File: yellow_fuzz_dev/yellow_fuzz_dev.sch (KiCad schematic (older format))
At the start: 150 parts

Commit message: woo boy I dunno buncha progress probably
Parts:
- removed C?: 27n, Capacitor_SMD:C_0603_1608Metric_Pad1.05x0.95mm_HandSolder, symbol Device:C
- removed C? (x2): 10n, Capacitor_SMD:C_0603_1608Metric_Pad1.05x0.95mm_HandSolder, symbol Device:C
- removed C?: 10p, Capacitor_SMD:C_0603_1608Metric_Pad1.05x0.95mm_HandSolder, symbol Device:C
- removed C? (x2): 1u, symbol Device:CP1
- removed C?: 100p, Capacitor_SMD:C_0603_1608Metric_Pad1.05x0.95mm_HandSolder, symbol Device:C
- removed C?: 220n, symbol Device:CP1
- removed C?: 47n, Capacitor_SMD:C_0603_1608Metric_Pad1.05x0.95mm_HandSolder, symbol Device:C
- removed C? (x3): 0.1u, Capacitor_SMD:C_0603_1608Metric_Pad1.05x0.95mm_HandSolder, symbol Device:C
- removed C?: 8.2n, Capacitor_SMD:C_0603_1608Metric_Pad1.05x0.95mm_HandSolder, symbol Device:C
- removed C?: 22n, Capacitor_SMD:C_0603_1608Metric_Pad1.05x0.95mm_HandSolder, symbol Device:C
- removed C?: 10u, symbol Device:CP1
- removed J?: PJ-202A, CUI_PJ-202A, symbol PJ-202A:PJ-202A
- removed R? (x3): 47k, Resistor_SMD:R_0603_1608Metric_Pad1.05x0.95mm_HandSolder, symbol Device:R
- removed R? (x5): 2.2k, Resistor_SMD:R_0603_1608Metric_Pad1.05x0.95mm_HandSolder, symbol Device:R
- removed R?: 22k, Resistor_SMD:R_0603_1608Metric_Pad1.05x0.95mm_HandSolder, symbol Device:R
- removed R? (x2): 330, Resistor_SMD:R_0603_1608Metric_Pad1.05x0.95mm_HandSolder, symbol Device:R
- removed R?: 100k, Resistor_SMD:R_0603_1608Metric_Pad1.05x0.95mm_HandSolder, symbol Device:R
- removed R?: 1M, Resistor_SMD:R_0603_1608Metric_Pad1.05x0.95mm_HandSolder, symbol Device:R
- removed RV?: R_POT_US, yellow_fuzz_dev:Potentiometer_Bourns_PCW1J_R24_B_Single_Vertical, symbol Device:R_POT_US
- removed RV? (x2): R_POT_Dual_Separate, yellow_fuzz_dev:Potentiometer_Bourns_PTV112_3417A_Dual_Vertical, symbol Device:R_POT_Dual_Separate
- removed RV? (x3): R_POT_US, yellow_fuzz_dev:Potentiometer_Bourns_PTV111_4420A_Single_Vertical, symbol Device:R_POT_US
- removed U? (x4): TL072CP, digikey-footprints:DIP-8_W7.62mm, symbol dk_opamps:TL072CP
- added C?: 10n, Capacitor_SMD:C_0603_1608Metric_Pad1.05x0.95mm_HandSolder, symbol Device:C
- added C?: 27n, Capacitor_SMD:C_0603_1608Metric_Pad1.05x0.95mm_HandSolder, symbol Device:C
- added C?: 0.1u, Capacitor_SMD:C_0603_1608Metric_Pad1.05x0.95mm_HandSolder, symbol Device:C
- added C?: 47n, Capacitor_SMD:C_0603_1608Metric_Pad1.05x0.95mm_HandSolder, symbol Device:C
- added J?: PJ-202A, digikey-footprints:Barrel_Jack_5.5mmODx2.1mmID_PJ-202A, symbol dk_Barrel-Power-Connectors:PJ-202A
- added Q?: BC817-25-TP, digikey-footprints:SOT-23-3, symbol yellow_fuzz_dev-rescue:BC817-25-TP-dk_NPN_Single
- added R?: 10k, Resistor_SMD:R_0603_1608Metric_Pad1.05x0.95mm_HandSolder, symbol Device:R
- added R? (x2): 2.2k, Resistor_SMD:R_0603_1608Metric_Pad1.05x0.95mm_HandSolder, symbol Device:R
- added R? (x2): 47k, Resistor_SMD:R_0603_1608Metric_Pad1.05x0.95mm_HandSolder, symbol Device:R
- added R?: 1k, Resistor_SMD:R_0603_1608Metric_Pad1.05x0.95mm_HandSolder, symbol Device:R
- added SW?: SW_SP3T_A24JP, yellow_fuzz_dev:A24JP, symbol yellow_fuzz_dev:SW_SP3T_A24JP
- added SW? (x2): SW_SPST_A11JP, yellow_fuzz_dev:A11JP, symbol yellow_fuzz_dev:SW_SPST_A11JP
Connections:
- net labels removed: LEVEL_OUT, TONE_IN, TONE_OUT
- wire segments 476 -> 389
- no-connect marks 0 -> 1
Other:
- note added: "333 Hz, Q = 4.6"
- note added: "4.9 kHz, Q = 2.2"
- note added: "First-order BPF (6 dB of cut at fc). \nfc = 200 Hz."
- note added: "HPF fc = 5 Hz"
- note added: "Returned pre-distortion boost:\n36dB centered at 224Hz, Q = 3.2."
- note added: "Stock pre-distortion boost:\n36dB centered at 1kHz, Q = 2.8."
- note added: "Three-position toggle implements \nSP3T when pins 3 and 5 are connected.\n\nUnused position removes filter from preboost."
- note added: "Tone"
- note added: "fc = 4 Hz"
- note removed: "High"
- note removed: "Level\n"
- note removed: "Low"
- note removed: "Mid Freq\n"
- note removed: "Mid\n"
- note removed: "Retuned pre-distortion boost filter."
- moved on the sheet: C?, D?, Q?, R?, RV?, S?, U?A, U?B

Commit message: moved footprints into PCB
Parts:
- removed C? (x3): 10u, symbol Device:CP1
- removed C? (x3): 1u, symbol Device:CP1
- removed C?: 100u, symbol Device:CP1
- removed R?: 220k, Resistor_SMD:R_0603_1608Metric_Pad1.05x0.95mm_HandSolder, symbol Device:R
- added C12: 100u, Capacitor_THT:CP_Radial_D5.0mm_P2.00mm, symbol Device:CP1
- added C17, C34, C37: 10u, Capacitor_THT:CP_Radial_D5.0mm_P2.00mm, symbol Device:CP1
- added C19, C26, C36: 1u, Capacitor_THT:CP_Radial_D4.0mm_P1.50mm, symbol Device:CP1
- added D5, D8: 1N34A, digikey:DO-35, symbol dk_Diodes-Rectifiers-Single:1N914BTR
- added D6, D9: WP7113QBC_D, digikey:LED_5mm_Radial, symbol yellow_fuzz_dev-rescue:WP7113QBC_D-dk_LEDs
- added POT1: 3386P-1-204TLF, yellow_fuzz_dev:3386P, symbol yellow_fuzz_dev:3386P-1-204TLF
- added POT2, POT3: 3362P-1-102TLF, yellow_fuzz_dev:3362P-1-102TLF, symbol yellow_fuzz_dev:3362P-1-102TLF
- added R16: 1k, Resistor_SMD:R_0603_1608Metric_Pad1.05x0.95mm_HandSolder, symbol Device:R
- added SW2, SW3: SW_SP3T_A24JP, yellow_fuzz_dev:A24JP, symbol yellow_fuzz_dev:SW_SP3T_A24JP
- BAT1: renamed from BAT?; footprint digikey-footprints:Battery_Holder_9V_BC9VPC-ND -> digikey:Battery_Holder_9V_BC9VPC-ND
- C1: renamed from C?; footprint (none) -> Capacitor_THT:CP_Radial_D4.0mm_P1.50mm
- C11, C15, C22, C8: renamed from C?; footprint (none) -> Capacitor_THT:CP_Radial_D5.0mm_P2.00mm
- CON1: renamed from CON?; footprint digikey-footprints:Headphone_Jack_6.35mm_SN49B12B -> digikey:Headphone_Jack_6.35mm_SN49B12B
- D3: renamed from D?; footprint digikey-footprints:LED_5mm_Radial -> digikey:LED_5mm_Radial
- D4, D7: renamed from D?; footprint digikey-footprints:Diode_DO-35_P10mm -> digikey:Diode_DO-35_P10mm
- J1: renamed from J?; footprint digikey-footprints:Barrel_Jack_5.5mmODx2.1mmID_PJ-202A -> digikey:Barrel_Jack_5.5mmODx2.1mmID_PJ-202A
- Q10, Q12, Q13, Q5, Q6, Q7, Q8, Q9: renamed from Q?; footprint digikey-footprints:SOT-23-3 -> digikey:SOT-23-3
- S1: renamed from S?; footprint digikey-footprints:Switch_Tactile_THT_6x6mm -> digikey:Switch_Tactile_THT_6x6mm
- U1, U2: renamed from U?; footprint digikey-footprints:DIP-8_W7.62mm -> digikey:DIP-8_W7.62mm
- gave numbers to parts that had none: 94
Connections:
- net +4V: now also C12.1
- net GND: now also C12.2, D5.K, D6.2, D8.A, D9.1
- net tone_block/TONE_OUT: now also C36.2
- net at C16.1, RV1.2, RV1.3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: now also C17.1
- net at C9.1, R17.2, U1.1: now also R16.1
- net at C9.2, SW1.2, U1.2: now also POT1.1 (CCW), POT1.2 (S)
- net at R23.2: now also C17.2
- net at R23.1, R26.2: now also POT2.1 (CCW), POT3.1 (CCW); no longer D4.2, D7.1
- net at R26.1, R27.1: now also C19.2
- net at R32.2, U2.3: now also C19.1
- net at Q9.2 (E), R35.1: now also C26.1
- net at Q11.1 (S), R40.2: now also C26.2
- net at Q13.1 (B), R48.2: now also C34.1
- net at Q11.2 (D), Q14.2 (D), R55.2: now also C34.2
- net at Q13.2 (E), R51.1: now also C37.1
- net at R53.1, R54.2: now also C37.2
- net at Q14.1 (S), R52.2: now also C36.1
- new net: D4.2, SW2.1
- new net: D7.1, SW3.1
- new net: POT2.2 (S), POT2.3 (CW), SW2.2
- new net: POT3.2 (S), POT3.3 (CW), SW3.2
- new net: POT1.3 (CW), R16.2
- new net: SW2.3, SW2.5
- new net: D5.A, SW2.4
- new net: D6.1, SW2.6
- new net: SW3.3, SW3.5
- new net: D8.K, SW3.4
- new net: D9.2, SW3.6
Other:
- note added: "200k Trim Pot lets us turn down the preboost, \nallowing us to take out op-amp clipping as much as we’d like."
- note added: "Let’s see if this takes the fizz out maybe."
- note added: "Three-position toggle implements \nSP3T when pins 3 and 5 are connected.\n\nNow you can A/B/C test diodes."
- moved on the sheet: C28, C29, C30, C31, C33, C35, D4, D7, Q10, Q12, R37, R39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

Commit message: added 3d to connector and DIP footprints, moved to project lib, updated PCB
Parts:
- removed BAT1: BC9VPC, digikey:Battery_Holder_9V_BC9VPC-ND, symbol dk_Battery-Holders-Clips-Contacts:BC9VPC
- removed CON1: SN49B12B, digikey:Headphone_Jack_6.35mm_SN49B12B, symbol yellow_fuzz_dev-rescue:SN49B12B-dk_Barrel-Audio-Connectors
- removed J1: PJ-202A, digikey:Barrel_Jack_5.5mmODx2.1mmID_PJ-202A, symbol dk_Barrel-Power-Connectors:PJ-202A
- removed POT2, POT3: 3362P-1-102TLF, yellow_fuzz_dev:3362P-1-102TLF, symbol yellow_fuzz_dev:3362P-1-102TLF
- removed S1: 1825910-6, digikey:Switch_Tactile_THT_6x6mm, symbol dk_Tactile-Switches:1825910-6
- removed U1, U2: TL072CP, digikey:DIP-8_W7.62mm, symbol dk_opamps:TL072CP
- added BAT1: BC9VPC, yellow_fuzz_dev:Battery_Holder_9V_BC9VPC-ND, symbol yellow_fuzz_dev:BC9VPC
- added J1: PJ-202A, yellow_fuzz_dev:Barrel_Jack_5.5mmODx2.1mmID_PJ-202A, symbol yellow_fuzz_dev:PJ-202A
- added J3: SN49B12B, yellow_fuzz_dev:Headphone_Jack_6.35mm_SN49B12B, symbol yellow_fuzz_dev:SN49B12B
- added P3, P4: 3362P-1-102TLF, yellow_fuzz_dev:3362PT, symbol yellow_fuzz_dev:3362P-1-102TLF
- added S1: 1825910-6, yellow_fuzz_dev:Switch_Tactile_THT_6x6mm, symbol yellow_fuzz_dev:1825910-6
- added U1, U2: TL072CP, yellow_fuzz_dev:DIP-8_W7.62mm, symbol yellow_fuzz_dev:TL072CP
- J2: Manufacturer Switchcraft Inc. -> (none); Manufacturer PN RA49B11 -> (none); Supplier Digi-Key -> (none); Supplier PN SC2546-ND -> (none)
- renumbered POT1 to P1, RV1 to P2
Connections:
- net +4V: now also U2.5
- net +9V: now also U1.8 (VCC+), U1.8 (VCC+), U2.8 (VCC+), U2.8 (VCC+)
- net GND: now also J3.S, S1.1, S1.2, U1.4 (VCC-), U1.4 (VCC-), U2.4 (VCC-), U2.4 (VCC-)
- net INPUT_RING: now also J3.R
- net SW_IN: now also S1.3, S1.4
- net at C16.1, C17.1, P2.2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: now also U1.7
- net at R1.2: now also J3.T
- net at C3.1, R13.2: now also U1.3
- net at C9.1, R16.1, R17.2: now also U1.1
- net at C14.1, R19.2: now also U1.5
- net at C16.2, R20.2, R21.1: now also U1.6
- net at R23.1, R26.2: now also P3.3 (CW), P4.3 (CW)
- net at C19.1, R32.2: now also U2.3
- net at C27.2, R36.1, R38.2: now also U2.6
- net at C24.1, R34.1, R36.2: now also U2.1
- net at C27.1, R38.1, R45.2: now also U2.7
- net at C24.2, R34.2, SW4.3 (B)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: now also U2.2
- net at Q3.3 (D): now also BAT1.NEG
- net at Q3.1 (G): now also BAT1.POS, J1.3
- net at Q1.1 (G), R5.1: now also J1.1
- net at Q1.3 (D): now also J1.2
- net at SW2.2: now also P3.1 (CCW), P3.2 (S)
- net at SW3.2: now also P4.1 (CCW), P4.2 (S)
- net at C9.2, P1.1 (CCW), P1.2 (S)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: now also U1.2

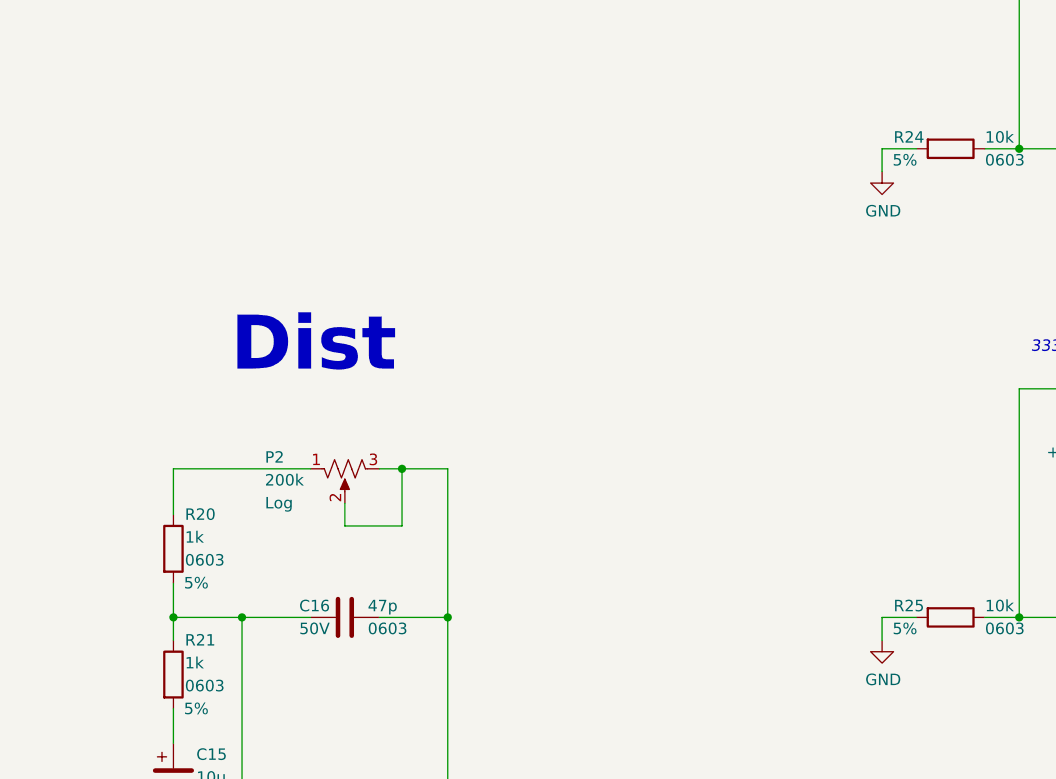
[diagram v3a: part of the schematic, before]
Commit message: updated potentiometers to use the same mechanical family throughout
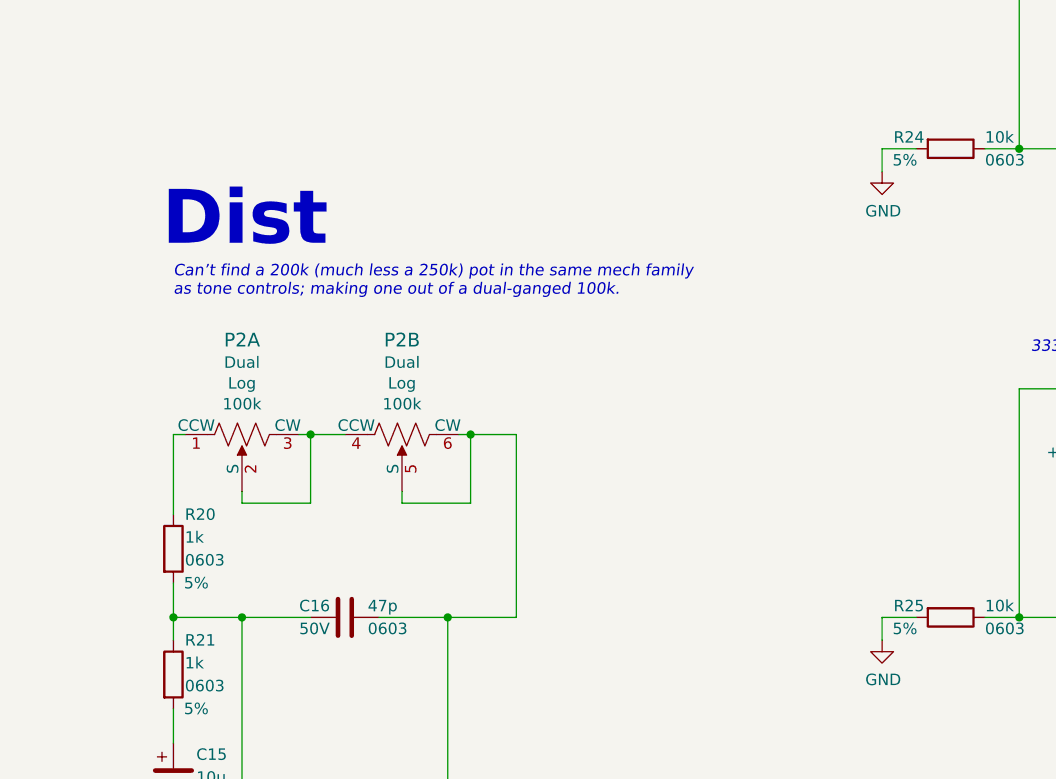
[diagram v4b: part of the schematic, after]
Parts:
- removed P2: R_POT_US, Potentiometer_THT:Potentiometer_Bourns_PTV09A-1_Single_Vertical, symbol Device:R_POT_US
- added P2: PTV112-4420A-A104, yellow_fuzz_dev:Potentiometer_Bourns_PTV112_3417A_Dual_Vertical, symbol yellow_fuzz_dev:PTV112-4420A-A104
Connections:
- net at R20.1: now also P2.1 (CCW)
- net at C16.1, C17.1, U1.7: now also P2.5 (S), P2.6 (CW)
- new net: P2.2 (S), P2.3 (CW), P2.4 (CCW)
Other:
- note added: "Can’t find a 200k (much less a 250k) pot in the same mech family\nas tone controls; making one out of a dual-ganged 100k."
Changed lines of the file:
@@
 	0    -1   -1   0
 $EndComp
-Text Notes 7800 7250 0    236  ~ 47
+Text Notes 7500 6700 0    236  ~ 47
 Dist
 $Comp
@@
 	1    0    0    -1
 $EndComp
-Wire Wire Line
-	8150 7650 7550 7650
-Connection ~ 8750 8300
-Connection ~ 8550 7650
-Wire Wire Line
-	8750 7650 8750 8300
-Wire Wire Line
-	8550 7650 8750 7650
-Wire Wire Line
-	8550 7650 8450 7650
-Wire Wire Line
-	8550 7900 8550 7650
-Wire Wire Line
-	8300 7900 8550 7900
-Wire Wire Line
-	8300 7800 8300 7900
 Connection ~ 16100 9950
 Wire Wire Line
@@
 	0    1    1    0
 $EndComp
-$Comp
-L Device:R_POT_US P2
-U 1 1 5E3629ED
-P 8300 7650
-F 0 "P2" V 8250 8000 50  0000 R CNN
-F 1 "R_POT_US" H 8233 7605 50  0001 R CNN
-F 2 "Potentiometer_THT:Potentiometer_Bourns_PTV09A-1_Single_Vertical" H 8300 7650 50  0001 C CNN
-F 3 "~" H 8300 7650 50  0001 C CNN
-F 4 "Bourns" H 8300 7650 50  0001 C CNN "Manufacturer"
-F 5 "PTV09A-4030U-A204" H 8300 7650 50  0001 C CNN "Manufacturer PN"
-F 6 "Mouser" H 8300 7650 50  0001 C CNN "Supplier"
-F 7 "652-PTV09A-4030UA204" H 8300 7650 50  0001 C CNN "Supplier PN"
-F 8 "Log" V 8450 8000 50  0000 R CNN "Taper"
-F 9 "200k" V 8350 8000 50  0000 R CNN "Value"
-	1    8300 7650
-	0    -1   1    0
-$EndComp
 Text Notes 950  1700 0    236  ~ 47
 Input
@@
 	1    0    0    -1
 $EndComp
-Wire Wire Line
-	7550 7650 7550 7850
 Wire Wire Line
 	7550 8150 7550 8300
@@
 	0    1    1    0
 $EndComp
+$Comp
+L yellow_fuzz_dev:PTV112-4420A-A104 P2
+U 1 1 5EB889C3
+P 8100 7500
+F 0 "P2" H 7850 7087 60  0000 C CNN
+F 1 "PTV112-4420A-A104" H 8290 7520 60  0001 L CNN
+F 2 "yellow_fuzz_dev:Potentiometer_Bourns_PTV112_3417A_Dual_Vertical" H 8300 7700 60  0001 L CNN
+F 3 "https://www.mouser.com/datasheet/2/54/PTVPTT-56034.pdf" H 8300 7800 60  0001 L CNN
+F 4 "Bourns" H 8300 7900 60  0001 L CNN "Manufacturer"
+F 5 "PTV112-4420A-A104" H 8300 8000 60  0001 L CNN "Manufacturer Part Number"
+F 6 "Mouser" H 8300 8100 60  0001 L CNN "Supplier"
+F 7 "652-PTV1124420AA104" H 8300 8200 60  0001 L CNN "Supplier Part Number"
+F 8 "Dual" H 7850 7185 50  0000 C CNN "Gangs"
+F 9 "Log" H 7850 7276 50  0000 C CNN "Taper"
+F 10 "100k" H 7850 7367 50  0000 C CNN "Resistance"
+	1    8100 7500
+	1    0    0    1
+$EndComp
+$Comp
+L yellow_fuzz_dev:PTV112-4420A-A104 P2
+U 2 1 5EB8AEC6
+P 8800 7500
+F 0 "P2" H 8550 7087 60  0000 C CNN
+F 1 "PTV112-4420A-A104" H 8990 7520 60  0001 L CNN
+F 2 "yellow_fuzz_dev:Potentiometer_Bourns_PTV112_3417A_Dual_Vertical" H 9000 7700 60  0001 L CNN
+F 3 "https://www.mouser.com/datasheet/2/54/PTVPTT-56034.pdf" H 9000 7800 60  0001 L CNN
+F 4 "Bourns" H 9000 7900 60  0001 L CNN "Manufacturer"
+F 5 "PTV112-4420A-A104" H 9000 8000 60  0001 L CNN "Manufacturer Part Number"
+F 6 "Mouser" H 9000 8100 60  0001 L CNN "Supplier"
+F 7 "652-PTV1124420AA104" H 9000 8200 60  0001 L CNN "Supplier Part Number"
+F 8 "Dual" H 8550 7185 50  0000 C CNN "Gangs"
+F 9 "Log" H 8550 7276 50  0000 C CNN "Taper"
+F 10 "100k" H 8550 7367 50  0000 C CNN "Resistance"
+	2    8800 7500
+	1    0    0    1
+$EndComp
+Wire Wire Line
+	7850 7750 7850 7800
+Wire Wire Line
+	7850 7800 8150 7800
+Wire Wire Line
+	8150 7800 8150 7500
+Wire Wire Line
+	8150 7500 8100 7500
+Wire Wire Line
+	8550 7750 8550 7800
+Wire Wire Line
+	8550 7800 8850 7800
+Wire Wire Line
+	8850 7800 8850 7500
+Wire Wire Line
+	8850 7500 8800 7500
+Wire Wire Line
+	7550 7850 7550 7500
+Wire Wire Line
+	7550 7500 7600 7500
+Wire Wire Line
+	8850 7500 9050 7500
+Wire Wire Line
+	9050 7500 9050 8300
+Wire Wire Line
+	9050 8300 8750 8300
+Connection ~ 8850 7500
+Connection ~ 8750 8300
+Wire Wire Line
+	8300 7500 8150 7500
+Connection ~ 8150 7500
+Text Notes 7550 6900 0    50   Italic 0
+Can’t find a 200k (much less a 250k) pot in the same mech family\nas tone controls; making one out of a dual-ganged 100k.
 $EndSCHEMATC

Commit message: first draft placement done. Added ampharos logo.
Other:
- note added: "Retuned pre-distortion boost:\n36dB centered at 224Hz, Q = 3.2."
- note removed: "Returned pre-distortion boost:\n36dB centered at 224Hz, Q = 3.2."
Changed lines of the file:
@@
 HPF fc = 5 Hz
 Text Notes 2150 7300 0    50   Italic 0
-Returned pre-distortion boost:\n36dB centered at 224Hz, Q = 3.2.
+Retuned pre-distortion boost:\n36dB centered at 224Hz, Q = 3.2.
 $Comp
 L Device:C C4
@@
 $EndComp
 $Comp
-L Device:R R25
-U 1 1 5E517E90
-P 10950 8300
-F 0 "R25" V 10900 8050 50  0000 L CNN
-F 1 "10k" V 10900 8450 50  0000 L CNN
-F 2 "Resistor_SMD:R_0603_1608Metric_Pad1.05x0.95mm_HandSolder" V 10880 8300 50  0001 C CNN
-F 3 "~" H 10950 8300 50  0001 C CNN
-F 4 "RC0603JR-071KL" H 10950 8300 50  0001 C CNN "Manufacturer PN"
-F 5 "5%" V 11000 8100 50  0000 C CNN "Tolerance"
-F 6 "Yageo" H 10950 8300 50  0001 C CNN "Manufacturer"
-F 7 "Digi-Key" H 10950 8300 50  0001 C CNN "Supplier"
-F 8 "311-1.0KGRCT-ND" H 10950 8300 50  0001 C CNN "Supplier PN"
-F 9 "0.1 W" H 10950 8300 50  0001 C CNN "Power"
-F 10 "0603" V 11000 8450 50  0000 L CNN "Package"
-	1    10950 8300
-	0    1    1    0
-$EndComp
-$Comp
 L yellow_fuzz_dev:+4V5 #PWR0162
 U 1 1 5E517E96
@@
 	12200 7300 12200 7450
 Wire Wire Line
-	11100 8300 11250 8300
-Wire Wire Line
 	11600 7300 11250 7300
 Wire Wire Line
 	11250 7300 11250 8300
-Connection ~ 11250 8300
 Wire Wire Line
 	11250 8300 12000 8300
-Wire Wire Line
-	10650 8400 10650 8300
-Wire Wire Line
-	10650 8300 10800 8300
-$Comp
-L power:GND #PWR0163
-U 1 1 5E517EAD
-P 10650 8400
-F 0 "#PWR0163" H 10650 8150 50  0001 C CNN
-F 1 "GND" H 10655 8227 50  0000 C CNN
-F 2 "" H 10650 8400 50  0001 C CNN
-F 3 "" H 10650 8400 50  0001 C CNN
-	1    10650 8400
-	1    0    0    -1
-$EndComp
 $Comp
 L power:+9V #PWR0164
@@
 P 8300 9950
 F 0 "U1" H 8500 9800 60  0000 L CNN
-F 1 "TL072CP" H 8500 9700 60  0000 L CNN
+F 1 "TL072CP" H 11700 9650 60  0000 L CNN
 F 2 "yellow_fuzz_dev:DIP-8_W7.62mm" H 8500 10150 60  0001 L CNN
 F 3 "http://www.ti.com/general/docs/suppproductinfo.tsp?distId=10&gotoUrl=http%3A%2F%2Fwww.ti.com%2Flit%2Fgpn%2Ftl071a" H 8500 10250 60  0001 L CNN
@@
 Text Notes 7550 6900 0    50   Italic 0
 Can’t find a 200k (much less a 250k) pot in the same mech family\nas tone controls; making one out of a dual-ganged 100k.
+Connection ~ 11250 8300
+$Comp
+L power:GND #PWR0163
+U 1 1 5E517EAD
+P 10650 8400
+F 0 "#PWR0163" H 10650 8150 50  0001 C CNN
+F 1 "GND" H 10655 8227 50  0000 C CNN
+F 2 "" H 10650 8400 50  0001 C CNN
+F 3 "" H 10650 8400 50  0001 C CNN
+	1    10650 8400
+	1    0    0    -1
+$EndComp
+Wire Wire Line
+	10650 8300 10800 8300
+Wire Wire Line
+	10650 8400 10650 8300
+Wire Wire Line
+	11100 8300 11250 8300
+$Comp
+L Device:R R25
+U 1 1 5E517E90
+P 10950 8300
+F 0 "R25" V 10900 8050 50  0000 L CNN
+F 1 "10k" V 10900 8450 50  0000 L CNN
+F 2 "Resistor_SMD:R_0603_1608Metric_Pad1.05x0.95mm_HandSolder" V 10880 8300 50  0001 C CNN
+F 3 "~" H 10950 8300 50  0001 C CNN
+F 4 "RC0603JR-071KL" H 10950 8300 50  0001 C CNN "Manufacturer PN"
+F 5 "5%" V 11000 8100 50  0000 C CNN "Tolerance"
+F 6 "Yageo" H 10950 8300 50  0001 C CNN "Manufacturer"
+F 7 "Digi-Key" H 10950 8300 50  0001 C CNN "Supplier"
+F 8 "311-1.0KGRCT-ND" H 10950 8300 50  0001 C CNN "Supplier PN"
+F 9 "0.1 W" H 10950 8300 50  0001 C CNN "Power"
+F 10 "0603" V 11000 8450 50  0000 L CNN "Package"
+	1    10950 8300
+	0    1    1    0
+$EndComp
 $EndSCHEMATC
